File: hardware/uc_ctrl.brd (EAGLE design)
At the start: 28 x 31 mm, 32 parts, among them Q4 si2305cd, Q7 si2305cd, T1 BC846, T3 BC846, Y1 32768Hz CFPX-217 12.5pF

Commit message: add pcb
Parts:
- removed C3: 100nF, rcl:C0805
- moved C2 65.5 mm to (23.8, 23.0)
- moved D2 44.1 mm to (5.20, 19.2), turned to 270 degrees
- moved U$9 39.7 mm to (2.30, 18.6), turned to 90 degrees
- moved U$5 38.7 mm to (2.30, 23.1), turned to 90 degrees
- moved U$3 36.1 mm to (2.30, 27.6), turned to 90 degrees
- moved U$7 30.1 mm to (23.6, 3.10)
- moved Q7 0.30 mm to (9.20, 24.4)
- moved R21 0.30 mm to (9.20, 20.9)
- moved T3 0.30 mm to (9.20, 17.8)
- moved C1 0.30 mm to (18.9, 27.7)
- moved Q4 0.30 mm to (18.9, 24.4)
- moved R19 0.30 mm to (18.9, 20.9)
- moved T1 0.30 mm to (18.9, 17.8)
- turned G1 to 270 degrees
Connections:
- net N$4 renamed UC_POW
- net 3V_CELL: now also U$9.2; no longer U$9.1
- net GND: no longer C3.1
- net PUSH: now also U$9.1; no longer U$9.2
- net UC_EN: now also U$1.18; no longer U$1.19
- net VCC: no longer C3.2
- net VCC_EN: now also U$1.19; no longer U$1.18
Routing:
- net 3V_CELL: track 0.00 -> 36.6 mm, vias 0 -> 4
- net PUSH: track 0.00 -> 26.3 mm, vias 0 -> 4
- net UC_POW: track 9.66 -> 19.4 mm, vias 0 -> 2
- net VCC: track 50.1 -> 56.4 mm
- net VCC_EN: track 0.00 -> 2.81 mm
- net P1.1: track 11.2 -> 13.8 mm
- net UC_EN: track 7.61 -> 6.67 mm
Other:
- board text added: "3Vext"
- board text added: "http://github.com/rodan/ucurrent_ctrl"
- board text added: "rev 1.0 201312"
- board text added: "sw"
- board text added: "uCurrent"
- board text removed: "avp"
- board text removed: "http://github.com/rodan/interphone"
- board text removed: "ip rev 2.0 201312"
- board text removed: "mp"
- board text removed: "px"

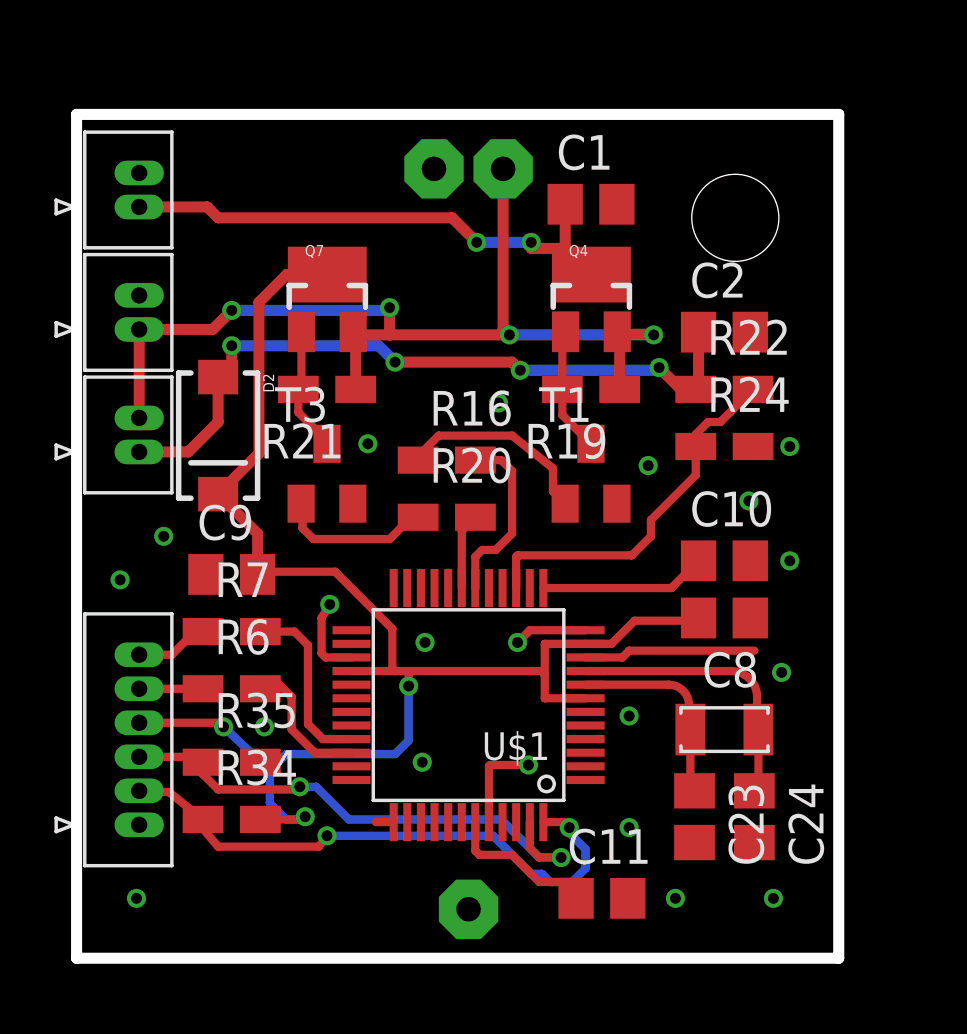
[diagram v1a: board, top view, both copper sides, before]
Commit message: also read uCurrent output voltage
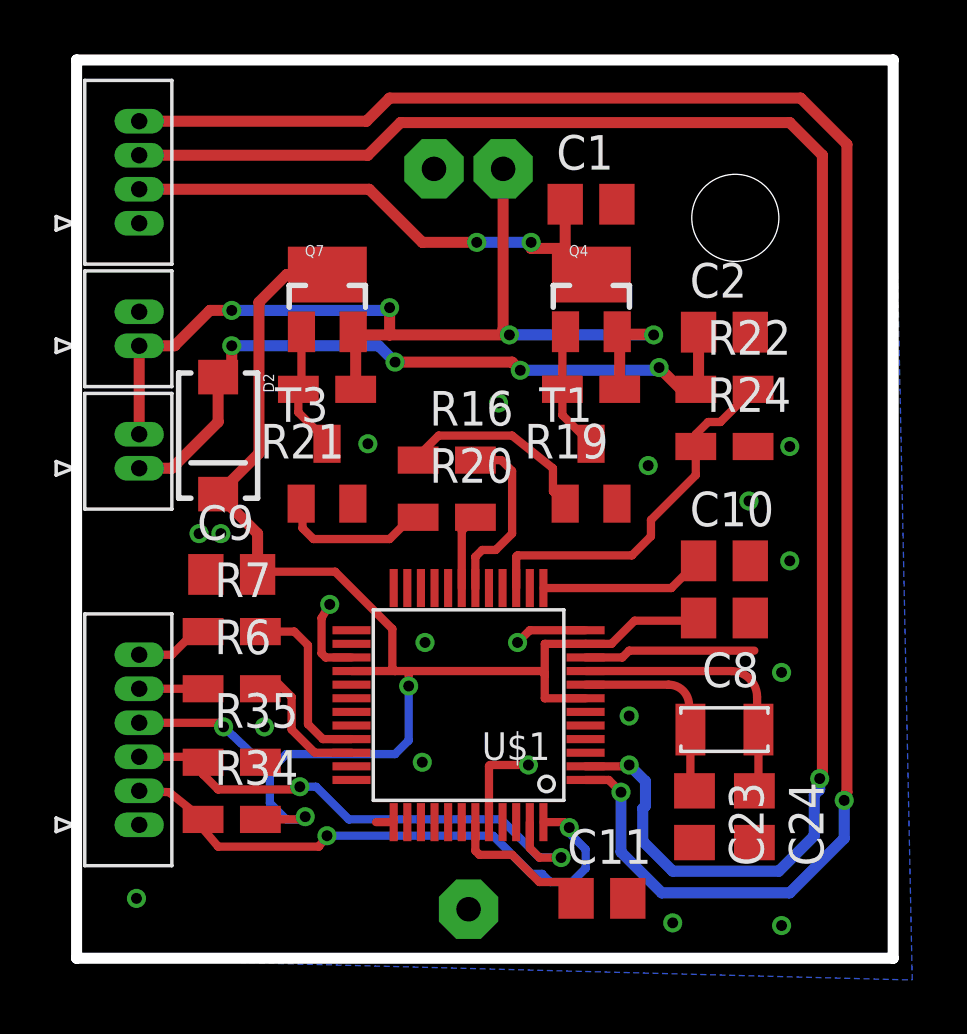
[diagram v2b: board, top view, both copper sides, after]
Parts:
- U$3: value ucurrent_pow -> ucurrent; device Simplex-Connectors:0530470210 -> Simplex-Connectors:0530470410
- moved U$3 0.60 mm to (2.30, 27.0)
- moved U$5 0.60 mm to (2.30, 22.5)
- moved U$9 0.60 mm to (2.30, 18.0)
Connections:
- new net P6.0: U$1.1, U$3.4
- new net P6.1: U$1.2, U$3.3
- net GND: now also U$3.1; no longer U$3.2
- net UC_POW: now also U$3.2; no longer U$3.1
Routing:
- net P6.0: track 0.00 -> 65.9 mm, vias 0 -> 2
- net P6.1: track 0.00 -> 63.2 mm, vias 0 -> 2
- net GND: vias 20 -> 19
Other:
- board size 28 x 31 mm -> 30 x 33 mm
- board text added: "3V"
- board text added: "Vcc"
- board text added: "Vout"
- board text added: "Vref"
- board text removed: "3Vext"

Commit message: rev 2
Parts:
- removed G1: HU2032-LF, Simplex-Battery:HU2032-LF
- removed U$9: push_button, Simplex-Connectors:0530470210
- added C3, C4, C7: 100nF, rcl:C0805
- added C5, C6: 10uF, rcl:C0805
- added LED2: green, led:CHIPLED_0805
- added R2: 100k, rcl:R0805W
- added SJ1: (no value), SparkFun-Passives:SJ_3_PASTE1&2
- added SJ2: SOLDERJUMPERNC2, SparkFun-Passives:SJ_2S-NOTRACE
- added U$4: SPST_TACTILE_SW, Simplex-Switches:6X3.5_TACTILE_SW
- added U$6: MOLEX_2HORIZONTAL, Simplex-Connectors:0530480210
- added U1: 3vLDO, SparkFun-PowerIC:SOT23-5
- U$2: device Simplex-Connectors:0530470610 -> Simplex-Connectors:0530480610
- U$3: value ucurrent -> MOLEX_4HORIZONTAL; device Simplex-Connectors:0530470410 -> Simplex-Connectors:0530480401
- U$5: value external_pow -> sw; device Simplex-Connectors:0530470210 -> Simplex-Connectors:0530480210
- moved U$3 49.9 mm to (45.9, 2.70), turned to 0 degrees
- moved U$5 43.9 mm to (41.5, 2.70), turned to 0 degrees
- moved Q7 37.1 mm to (43.0, 9.20), turned to 180 degrees
- moved D2 35.9 mm to (38.1, 4.90), turned to 90 degrees
- moved C1 35.2 mm to (52.0, 15.8), turned to 90 degrees
- moved R21 34.8 mm to (43.0, 12.7), turned to 0 degrees
- moved R16 34.7 mm to (48.3, 19.0), turned to 180 degrees
- moved T3 33.9 mm to (43.0, 15.8), turned to 180 degrees
- moved Q4 33.1 mm to (48.3, 9.20), turned to 180 degrees
- moved R19 30.5 mm to (48.3, 12.7), turned to 0 degrees
- moved R20 29.5 mm to (43.0, 19.0), turned to 180 degrees
- moved T1 29.5 mm to (48.3, 15.8), turned to 180 degrees
- moved C2 22.9 mm to (34.3, 2.70), turned to 180 degrees
- moved R22 19.2 mm to (34.3, 4.80), turned to 180 degrees
- moved R24 15.9 mm to (34.3, 6.90)
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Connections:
- net P6.0 renamed VREF
- net P6.1 renamed VOUT
- removed net 3V_CELL: G1.+, Q4.2, Q7.2, R19.1, R21.1, U$5.1, U$9.2
- removed net P1.1: R22.2, R24.1, U$1.15
- new net N$1: LED2.C, R2.2
- new net N$2: LED2.A, U$1.22
- new net N$4: C6.1, C7.1, D2.C, Q7.3, SJ2.1, U1.1, U1.3
- new net N$5: C3.1, U1.4
- new net N$8: Q4.2, R19.1, SJ1.2
- new net VBAT: R22.2, R24.1, U$1.15, U$1.3
- new net VCC_IN: Q7.2, R21.1, SJ1.3, U$4.1, U$5.P$2, U$6.P$2
- net GND: now also C3.2, C4.2, C5.2, C6.2, C7.2, R2.1, U$6.P$1, U1.2; no longer G1.-, U$5.2
- net PUSH: now also U$4.2, U$5.P$1; no longer U$9.1
- net UC_EN: now also U$1.19; no longer U$1.18
- net VCC: now also C4.1, C5.1, SJ1.1, SJ2.2, U1.5; no longer D2.C, Q7.3
- net VCC_EN: now also U$1.18; no longer U$1.19
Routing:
- net VCC_IN: track 0.00 -> 46.5 mm, vias 0 -> 2
- net VREF: track 65.9 -> 27.0 mm, vias 2 -> 0
- net VOUT: track 63.2 -> 25.3 mm, vias 2 -> 0
- net 3V_CELL: track 36.9 -> 0.00 mm, vias 4 -> 0
- net N$4: track 0.00 -> 36.8 mm, vias 0 -> 1
- net UC_EN: track 6.67 -> 30.7 mm, vias 0 -> 2
- net VBAT: track 0.00 -> 21.5 mm, vias 0 -> 2
- net TEST: track 19.9 -> 41.1 mm
- net RST: track 21.3 -> 41.8 mm, vias 2 -> 0
- net VCC_EN: track 2.81 -> 22.4 mm, vias 0 -> 2
- net VCC: track 56.4 -> 71.2 mm, vias 3 -> 6
- net P1.1: track 13.8 -> 0.00 mm
- net N$8: track 0.00 -> 10.0 mm, vias 0 -> 1
- net N$2: track 0.00 -> 6.66 mm
- net N$3: track 7.32 -> 2.12 mm
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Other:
- board size 30 x 33 mm -> 62.5 x 23 mm
- board text added: "1"
- board text added: "2"
- board text added: "SJ1"
- board text added: "SJ2"
- board text added: "VBAT+ out"
- board text added: "VBAT- out"
- board text added: "Vcc_in"
- board text added: "Vout+ in"
- board text added: "Vout- in"
- board text added: "battery"
- board text added: "debug"
- board text added: "ext_sw"
- board text added: "if Vcc_in is between 2.8-3.0 V SJ1 - short open SJ2 - short if Vcc_in is between 3.1-5.0V SJ1 - open short SJ2 - open"
- board text added: "rev 2.0 201312"
- board text removed: "3V"
- board text removed: "Vcc"
- board text removed: "Vout"
- board text removed: "Vref"
- board text removed: "rev 1.0 201312"
- board text removed: "sw"

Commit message: cleanup
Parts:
- added U$8: RESETTABLE, Simplex-Fuses:1210
- R16, R20: value 100k -> 100K
- R19, R21: value 47k -> 220K
- R22: value 1K -> 500K
- SJ1: value (none) -> pow
- U$3: value MOLEX_4HORIZONTAL -> uCurrent
- U$6: value MOLEX_2HORIZONTAL -> power
- moved C11 1.10 mm to (15.5, 3.50)
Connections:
- new net N$9: U$6.P$2, U$8.P$2
- net VCC_IN: now also U$8.P$1; no longer U$6.P$2
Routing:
- net GND: track 15.0 -> 40.9 mm, vias 39 -> 41
- net N$9: track 0.00 -> 6.45 mm
- net N$7: track 8.07 -> 9.17 mm
- net VCC_IN: track 46.5 -> 45.8 mm
- net RST: track 41.8 -> 41.3 mm

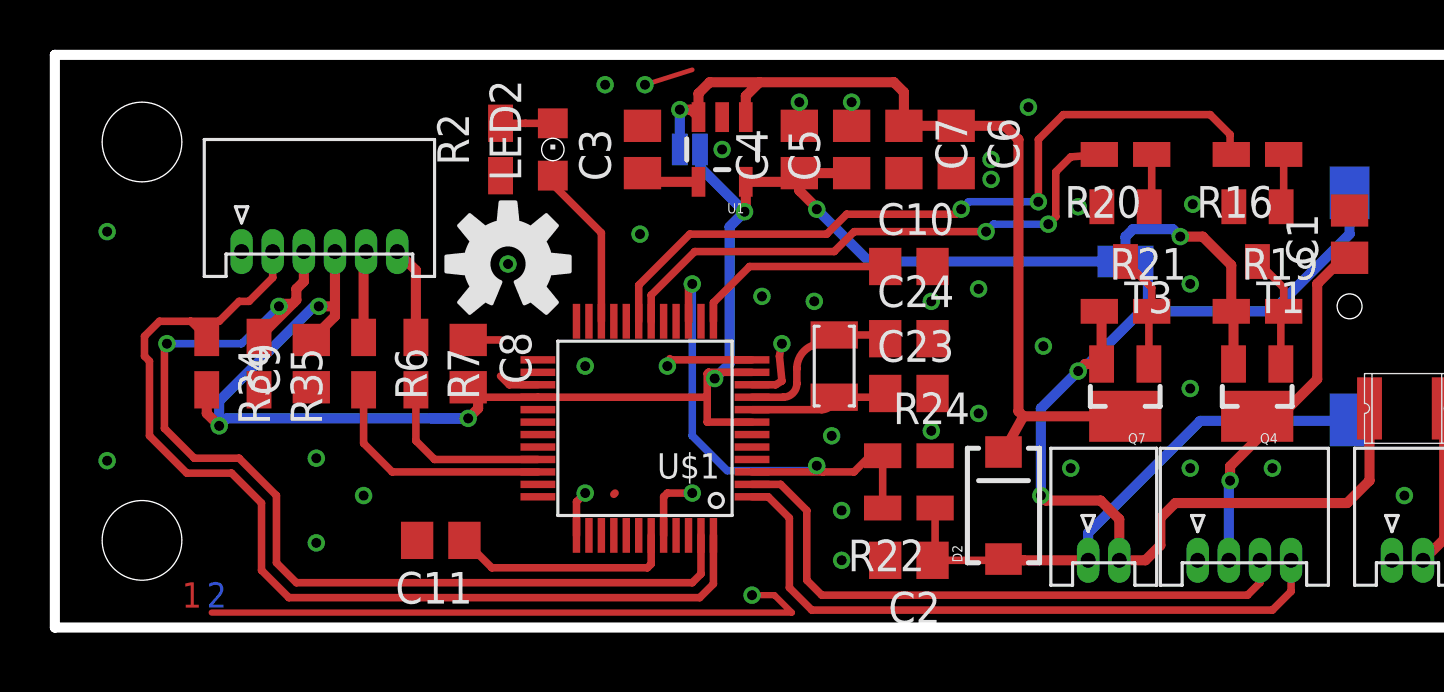
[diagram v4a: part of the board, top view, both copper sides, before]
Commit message: add 16bit adc
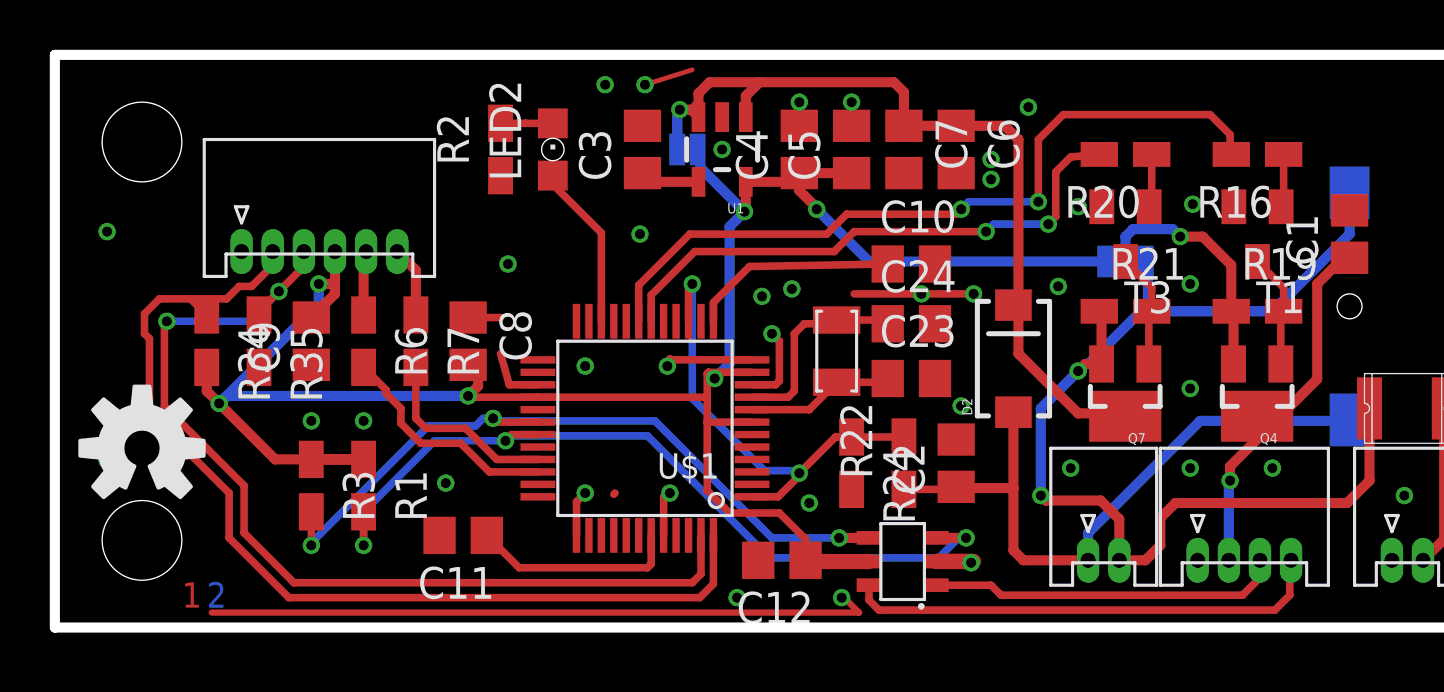
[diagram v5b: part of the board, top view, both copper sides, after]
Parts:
- added C12: 100nF, rcl:C0805
- added R1: DNP 10k, rcl:R0805W
- added R3: 10k, rcl:R0805W
- added U$9: ADS1110, Simplex-ICs:SOT23-6
- R22: value 500K -> 390K
- moved U$7 16.5 mm to (3.50, 7.20)
- moved D2 5.91 mm to (38.5, 10.8)
- moved C2 4.34 mm to (36.2, 6.60), turned to 90 degrees
- moved R24 2.32 mm to (32.0, 6.60), turned to 270 degrees
- moved R22 1.81 mm to (34.1, 6.60), turned to 90 degrees
- moved C11 0.92 mm to (16.4, 3.70)
- moved C8 0.90 mm to (16.6, 11.5)
- moved C9 0.90 mm to (10.3, 11.5)
- moved R34 0.90 mm to (6.10, 11.5)
- moved R35 0.90 mm to (8.20, 11.5)
- moved R6 0.90 mm to (12.4, 11.5)
- moved R7 0.90 mm to (14.5, 11.5)
- moved C23 0.61 mm to (34.4, 10.0)
- moved C24 0.61 mm to (34.4, 12.2)
- moved Y1 0.61 mm to (31.4, 11.1)
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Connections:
- new net SCL: R1.2, U$1.31, U$9.3
- new net SDA: R3.2, U$1.30, U$9.4
- net GND: now also C12.2, U$9.2
- net VBAT: now also U$1.1; no longer U$1.3
- net VCC: now also C12.1, R1.1, R3.1, U$9.5
- net VOUT: now also U$9.1; no longer U$1.2
- net VREF: now also U$9.6; no longer U$1.1
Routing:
- net SCL: track 0.00 -> 33.1 mm, vias 0 -> 3
- net SDA: track 0.00 -> 29.8 mm, vias 0 -> 3
- net VCC: track 71.4 -> 90.6 mm
- net VOUT: track 25.0 -> 14.2 mm
- net GND: track 40.9 -> 50.7 mm, vias 41 -> 40
- net VREF: track 26.7 -> 19.3 mm
- net PUSH: track 22.7 -> 26.7 mm
- net VBAT: track 21.5 -> 18.9 mm
- net N$4: track 36.8 -> 34.2 mm
- net TEST: track 41.0 -> 39.2 mm
- net N$25: track 6.80 -> 8.31 mm
- net TX: track 3.76 -> 2.86 mm
- net RX: track 3.49 -> 2.59 mm
- net N$7: track 9.17 -> 8.35 mm
- net RST: track 41.3 -> 40.5 mm
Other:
- board text added: "if Vcc_in is between 2.8-3.0 V SJ1 - short open SJ2 - short if Vcc_in is between 3.1-4.0V SJ1 - open short SJ2 - open"
- board text removed: "if Vcc_in is between 2.8-3.0 V SJ1 - short open SJ2 - short if Vcc_in is between 3.1-5.0V SJ1 - open short SJ2 - open"

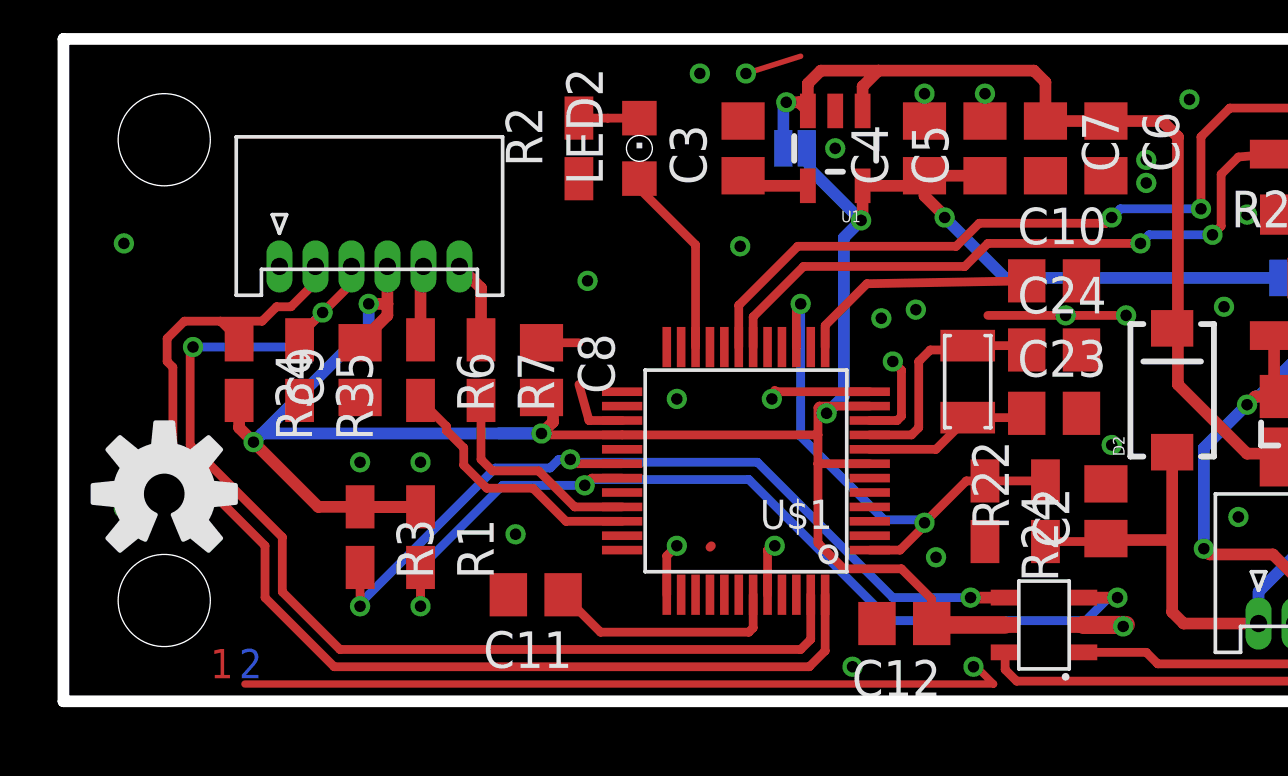
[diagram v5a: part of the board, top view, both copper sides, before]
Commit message: sent gerbers to manufacturer
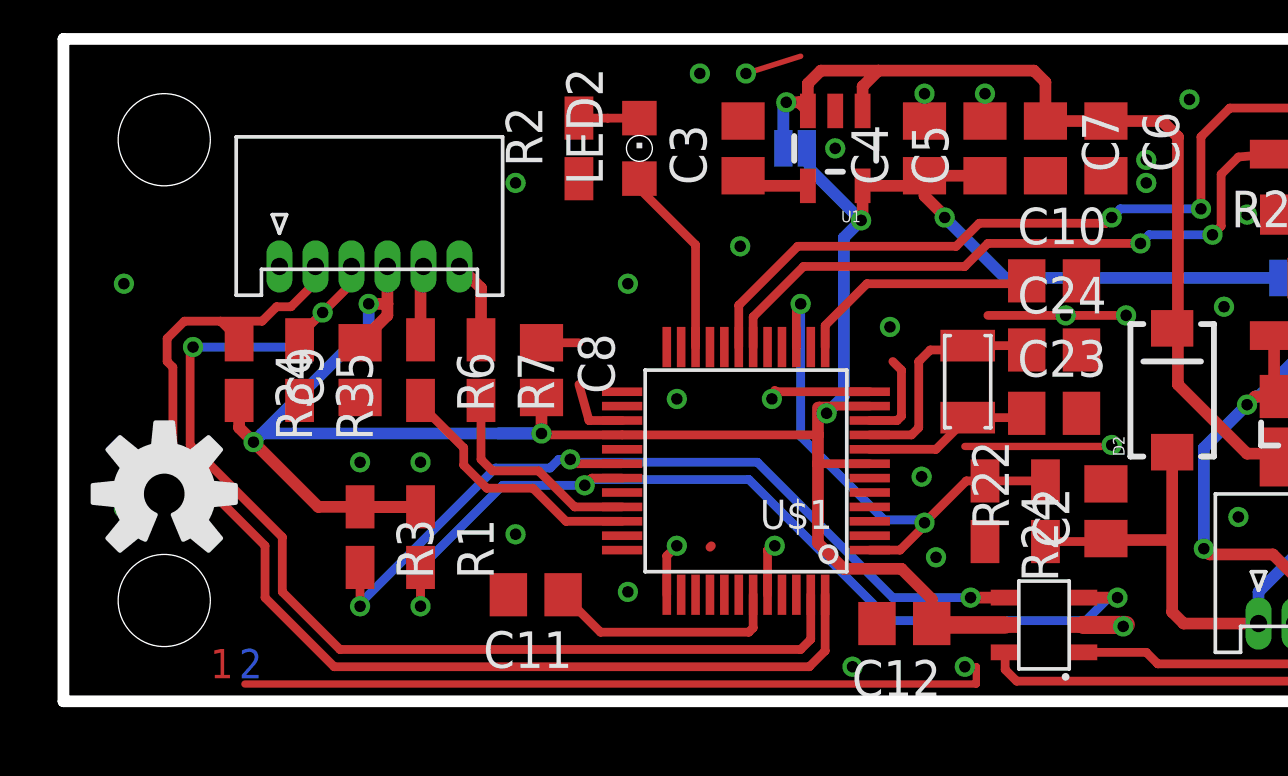
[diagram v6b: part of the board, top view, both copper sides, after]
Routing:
- net GND: track 50.7 -> 55.3 mm, vias 40 -> 41
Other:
- board text added: "if Vcc_in is between 2.8-3.0 V SJ1 - short open SJ2 - short if Vcc_in is between 3.1-4.2V SJ1 - open short SJ2 - open"
- board text removed: "if Vcc_in is between 2.8-3.0 V SJ1 - short open SJ2 - short if Vcc_in is between 3.1-4.0V SJ1 - open short SJ2 - open"
